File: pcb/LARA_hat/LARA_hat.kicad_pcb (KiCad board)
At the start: 2 copper layers, 65 x 56 mm, 33 parts, among them J1 Raspberry_Pi_4, J2 Conn_RoboClaw, J3 Conn_Dynamixel, J4 Conn_01x02_Pin, J5 12V in, J6 LED_JST, J7 I2C_JST, U1 MCP2515-xSO, U2 SN65HVD230, U3 74LVC2G241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

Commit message: pcb
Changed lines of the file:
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@@
 		(tenting front back)
 		(pcbplotparams
-			(layerselection 0x00000000_00000000_55555555_575555ff)
+			(layerselection 0x00000000_00000000_55555555_5755f5ff)
 			(plot_on_all_layers_selection 0x00000000_00000000_00000000_00000000)
 			(disableapertmacros no)
-			(usegerberextensions no)
+			(usegerberextensions yes)
 			(usegerberattributes yes)
 			(usegerberadvancedattributes yes)
-			(creategerberjobfile yes)
+			(creategerberjobfile no)
 			(dashed_line_dash_ratio 12.000000)
 			(dashed_line_gap_ratio 3.000000)
@@
 		(tags "LED handsolder")
 		(property "Reference" "D1"
-			(at 0 -1.65 0)
+			(at 2.7876 -0.0356 0)
 			(layer "F.SilkS")
 			(effects
@@
 		(tags "capacitor handsolder")
 		(property "Reference" "C2"
-			(at 0 -1.68 0)
+			(at -2.8972 -0.092 0)
 			(layer "F.SilkS")
 			(effects
@@
 		(tags "LED handsolder")
 		(property "Reference" "D2"
-			(at 0 -1.65 0)
+			(at 2.931 -0.0384 0)
 			(layer "F.SilkS")
 			(effects
@@
 		(tags "resistor handsolder")
 		(property "Reference" "R7"
-			(at 0 -1.65 0)
+			(at 2.8464 -0.0124 0)
 			(layer "F.SilkS")
 			(effects
@@
 		(tags "capacitor handsolder")
 		(property "Reference" "C1"
-			(at 0 -1.68 0)
+			(at -2.7876 0.1428 0)
 			(layer "F.SilkS")
 			(effects
@@
 		(tags "resistor handsolder")
 		(property "Reference" "R6"
-			(at 0 -1.65 0)
+			(at 2.8464 -0.066 0)
 			(layer "F.SilkS")
 			(effects

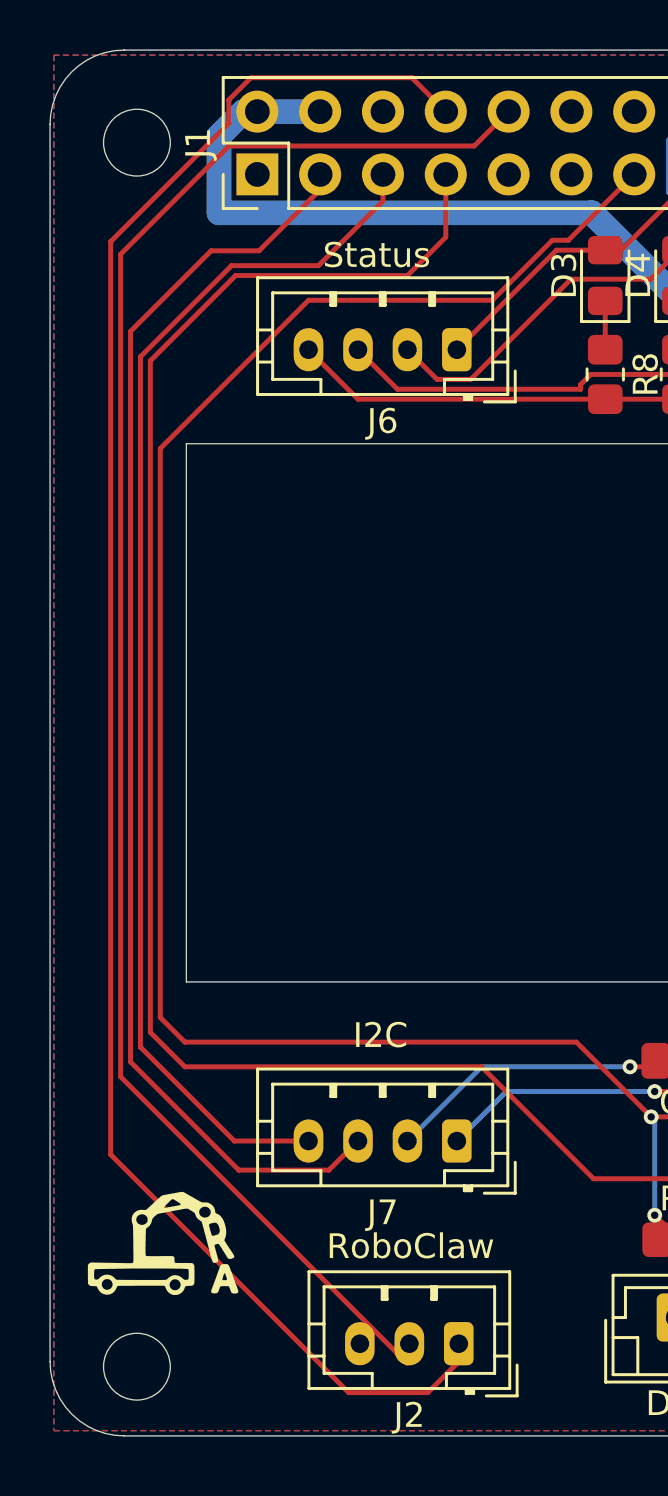
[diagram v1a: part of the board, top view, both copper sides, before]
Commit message: pcb error fixed
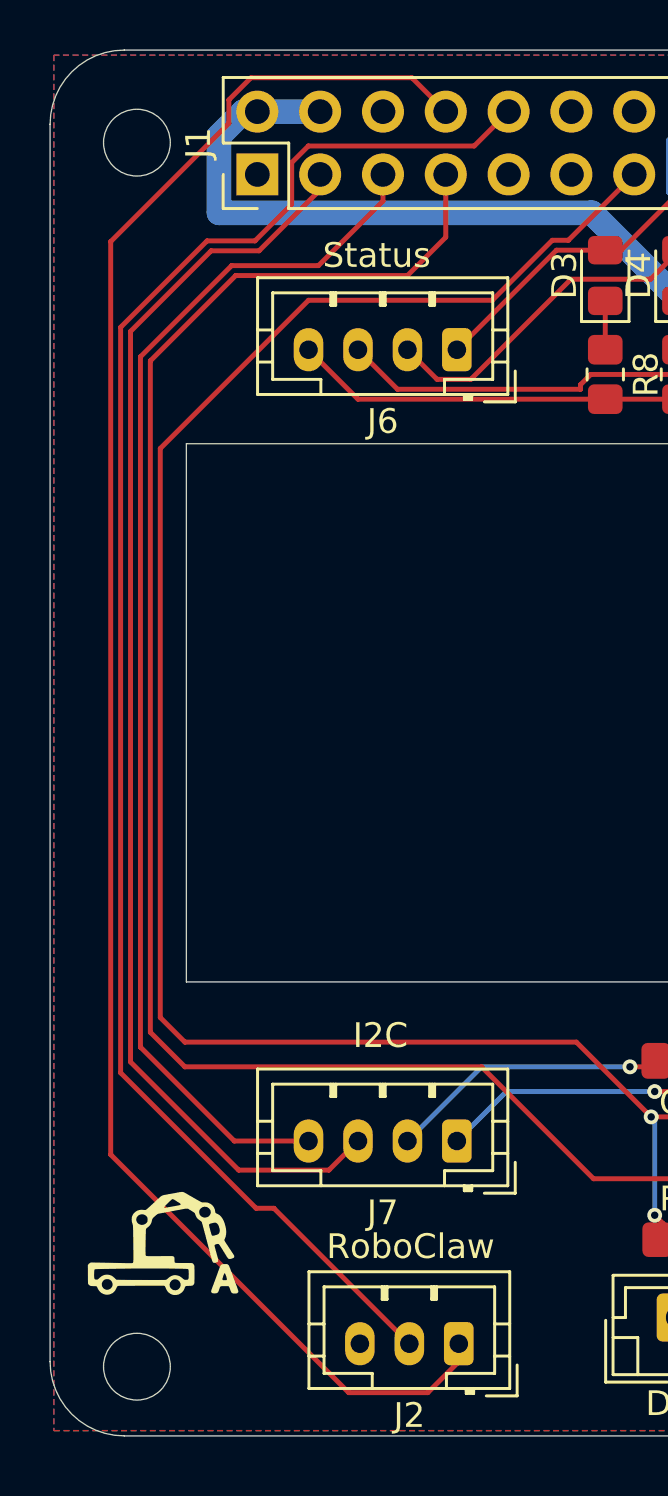
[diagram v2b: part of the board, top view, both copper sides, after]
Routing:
- net Net-(J1-GPIO15/UART_RXD): track 67.7 -> 66.6 mm
